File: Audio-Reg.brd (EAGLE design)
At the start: 20.3 x 25.4 mm, 18 parts, among them IC1 3.3V, Q1 NPN2SC3422-2, Q2 NPN2SC3325, Q3 PNP2SA1313

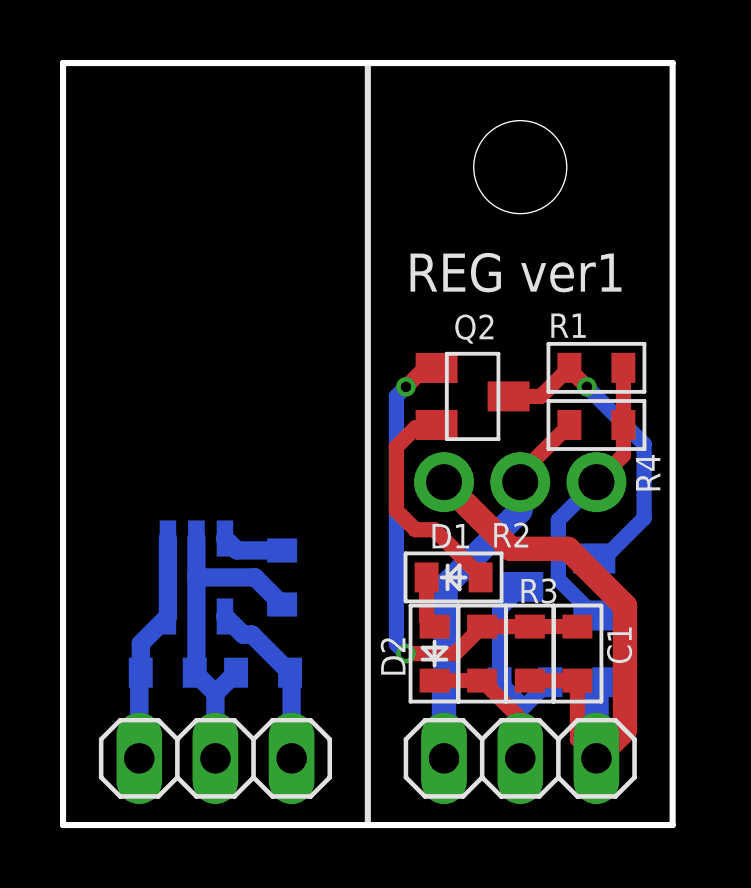
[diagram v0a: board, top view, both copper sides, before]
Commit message: 回路図を修正
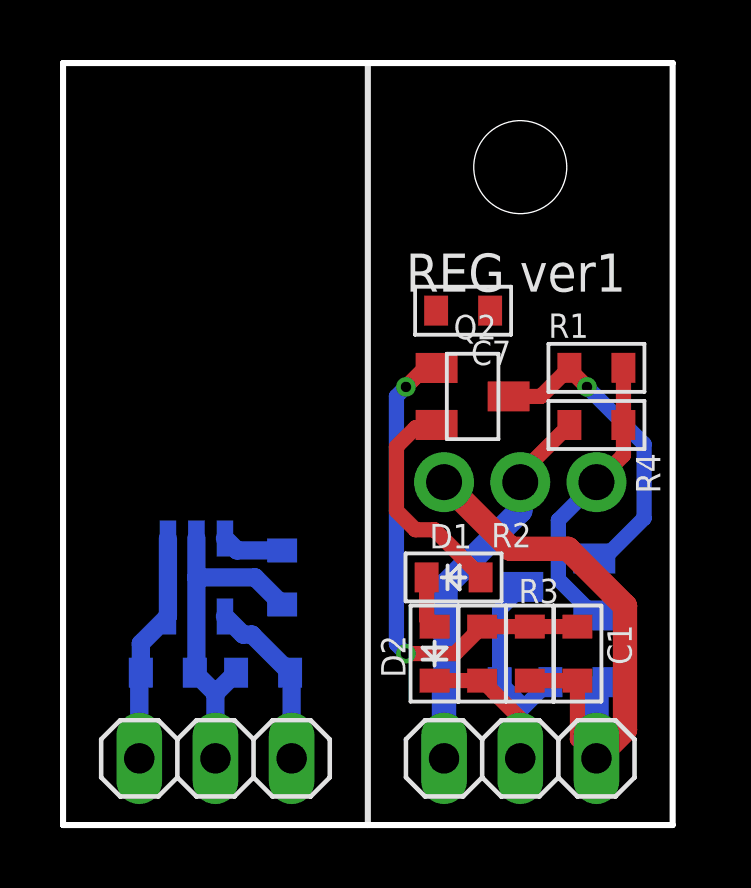
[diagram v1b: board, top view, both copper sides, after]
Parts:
- added C7: 100p, my_rcl:1608
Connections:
- net N$10: now also C7.1
- net N$3: now also C7.2
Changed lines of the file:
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@@
 <?xml version="1.0" encoding="utf-8"?>
 <!DOCTYPE eagle SYSTEM "eagle.dtd">
-<eagle version="9.6.1">
+<eagle version="9.6.2">
 <drawing>
 <settings>
@@
 <attribute name="VALUE" x="19.38" y="15.135" size="0.8128" layer="27" rot="R180"/>
 </element>
+<element name="C7" library="my_rcl" package="1608" value="100p" x="13.335" y="17.145" smashed="yes" rot="R180">
+<attribute name="NAME" x="14.935" y="16.145" size="0.8128" layer="25" rot="R180"/>
+<attribute name="VALUE" x="14.935" y="18.945" size="0.8128" layer="27" rot="R180"/>
+</element>
 </elements>
 <signals>
@@
 <wire x1="11.43" y1="14.605" x2="11.1125" y2="14.2875" width="0.508" layer="16"/>
 <wire x1="11.1125" y1="14.2875" x2="11.1125" y2="6.0325" width="0.508" layer="16"/>
+<contactref element="C7" pad="2"/>
+<wire x1="12.4525" y1="15.2375" x2="12.435" y2="17.145" width="0" layer="19" extent="1-1"/>
 </signal>
 <signal name="OUT">
@@
 <wire x1="19.3675" y1="10.2275" x2="18.0275" y2="8.8875" width="0.508" layer="16"/>
 <wire x1="19.3675" y1="12.7" x2="19.3675" y2="10.2275" width="0.508" layer="16"/>
+<contactref element="C7" pad="1"/>
+<wire x1="14.8525" y1="14.2875" x2="14.235" y2="17.145" width="0" layer="19" extent="1-1"/>
 </signal>
 </signals>
